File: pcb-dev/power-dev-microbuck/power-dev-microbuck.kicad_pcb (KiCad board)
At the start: 2 copper layers, 21 x 11 mm, 30 parts, among them J1 Pin headers, J2 Pin headers, U1 TPS563200, U2 TPS563200

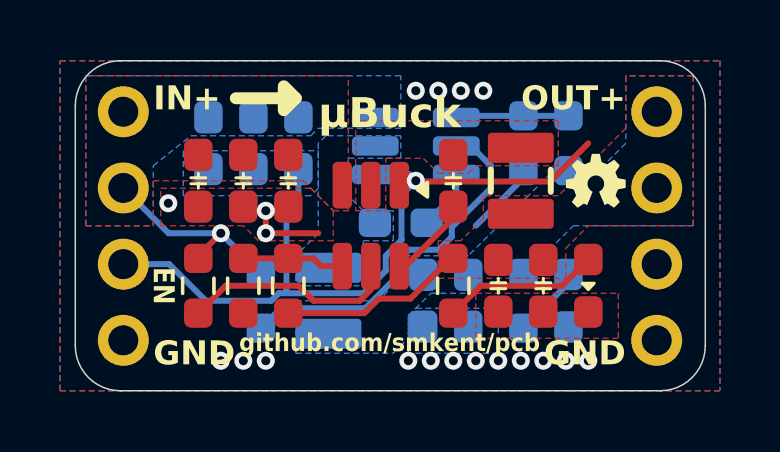
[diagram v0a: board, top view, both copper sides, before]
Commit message: Add WA icon to jig boards, square ground pads on μbuck/μboost
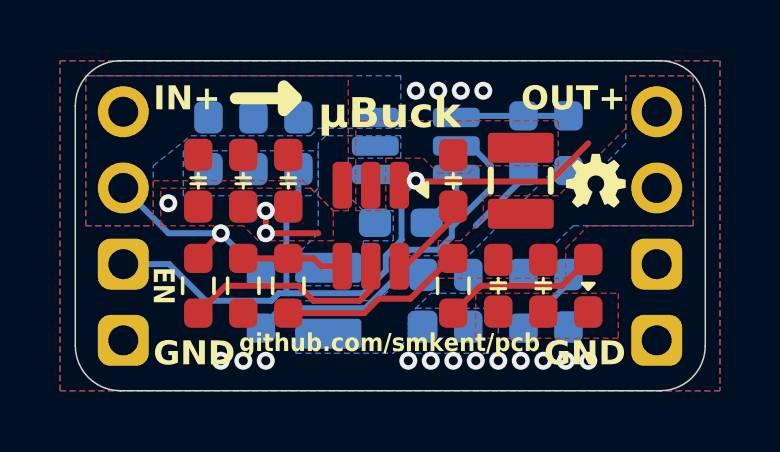
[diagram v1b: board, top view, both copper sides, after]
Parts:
- added G***: LOGO, graphics:wa-state-heart-2mm, B.Cu at (107.2, 70.0)
- J1, J2: footprint custom:PinHeader_1x04_P2.54mm_Vertical_simple -> custom:PinHeader_1x04_P2.54mm_Vertical_simple_pad3,4gnd
